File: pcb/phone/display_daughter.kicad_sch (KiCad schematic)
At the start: 5 parts

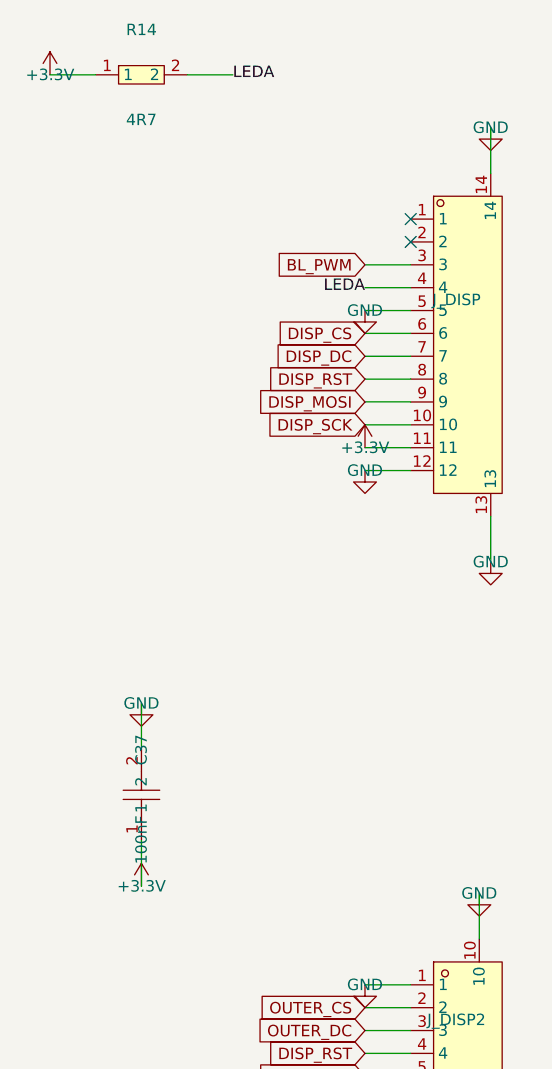
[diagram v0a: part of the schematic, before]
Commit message: User edits: keypad rewiring, sheet reorder, ERC severity reverts, R24 fix
Keypad (keypad.kicad_sch):
- Rotated all 20 switches 270 degrees for vertical contact orientation
- Wired all 4 pins on each switch (pins 1&2 to column, pins 3&4 to row)
- Removed all 37 no_connect markers on pins 3&4
- Cleaned up to 25.4mm (1-inch) grid spacing
- Added pull-down resistors to all 4 columns (was only KEY_COL3)

Root sheet (phone.kicad_sch):
- Reordered sub-sheet blocks (Display_Daughter before SIM_SD)
- Cleaned up PWR_FLAG symbol formatting/indentation
- Reordered PWR_FLAG and +BATT symbol placement

MCU sheet (mcu.kicad_sch):
- Repositioned +3.3V power symbol (#PWR32) at pin 190.5,200.66

Project settings (phone.kicad_pro):
- Reverted ERC suppressions: endpoint_off_grid, isolated_pin_label,
  lib_symbol_mismatch back to warning (want actual fixes, not ignores)
- Added SW2-20 to used designators
- Reordered sheets list (Display_Daughter before SIM_SD)

Other sheets (codec, display, display_daughter, sim_sd):
- KiCad editor reformatting upon save

Generated with [Devin](https://devin.ai)

Co-Authored-By: Devin <158243242+devin-ai-integration[bot]@users.noreply.github.com>
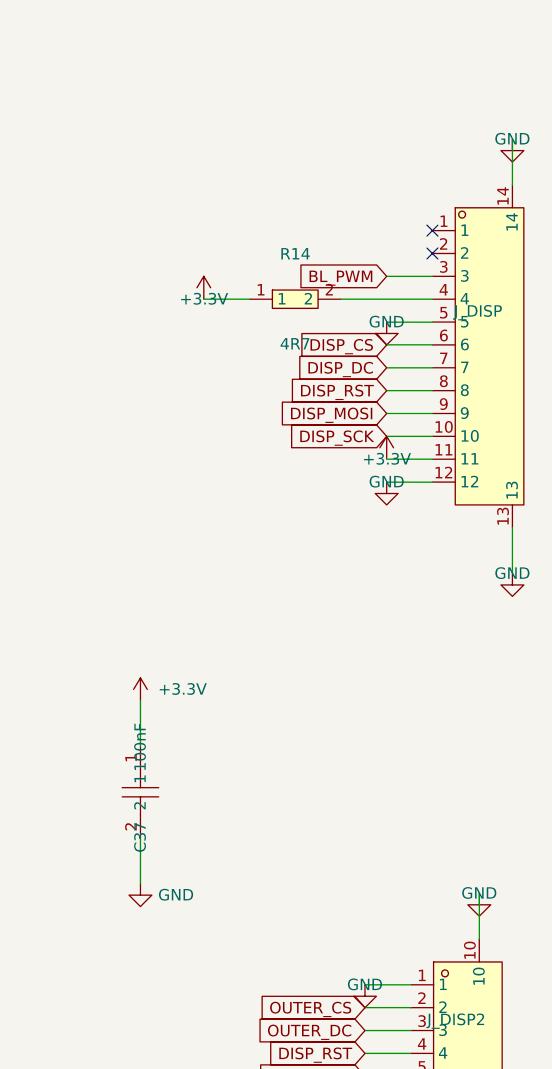
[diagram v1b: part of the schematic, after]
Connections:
- net LEDA: no longer names the net of J_DISP.4, R14.2
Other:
- moved on the sheet: C37, J_DISP, R14

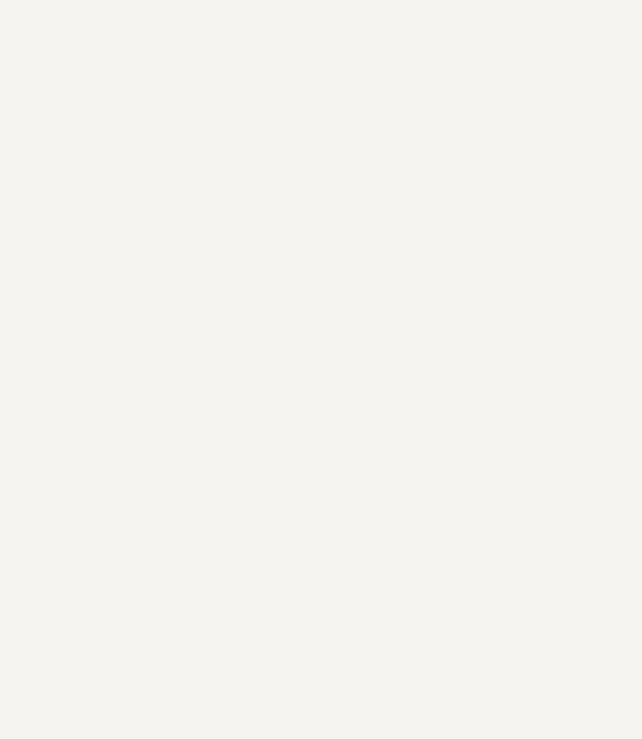
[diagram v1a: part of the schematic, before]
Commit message: Add J_HINGE2 hinge connector to display daughterboard
The display daughterboard (display_daughter.kicad_sch) was missing its
hinge connector — it had J_DISP, J_DISP2, and J_EARPIECE but no connector
to receive the flex cable from the main board's J_HINGE.

Added J_HINGE2 (connectors:0.5K-HX-14PWB, 14-pin 0.5mm FPC) at (130, 130)
with the same pin-to-net mapping as J_HINGE on the main board:

  Pin 1: +3.3V       Pin 8: OUTER_CS     Pin 15: GND (mounting)
  Pin 2: GND         Pin 9: OUTER_DC     Pin 16: GND (mounting)
  Pin 3: DISP_MOSI   Pin 10: BL_PWM
  Pin 4: DISP_SCK    Pin 11: NC (spare)
  Pin 5: DISP_CS     Pin 12: EARPIECE+
  Pin 6: DISP_DC     Pin 13: EARPIECE-
  Pin 7: DISP_RST    Pin 14: GND

All signal pins connect to existing global labels on the daughterboard
sheet (DISP_MOSI, DISP_SCK, DISP_CS, DISP_DC, DISP_RST, OUTER_CS,
OUTER_DC, BL_PWM, EARPIECE+, EARPIECE-). Power pins connect to +3.3V
and GND power symbols. Pin 11 (spare) has a no_connect marker.

Also added the 0.5K-HX-14PWB lib_symbol definition to the daughterboard
sheet (extracted from display.kicad_sch).

ERC: 0 errors, 196 warnings (152 endpoint_off_grid from FPC pin pitch,
35 lib_symbol_mismatch pre-existing, 9 isolated_pin_label pre-existing).

Generated with [Devin](https://devin.ai)

Co-Authored-By: Devin <158243242+devin-ai-integration[bot]@users.noreply.github.com>
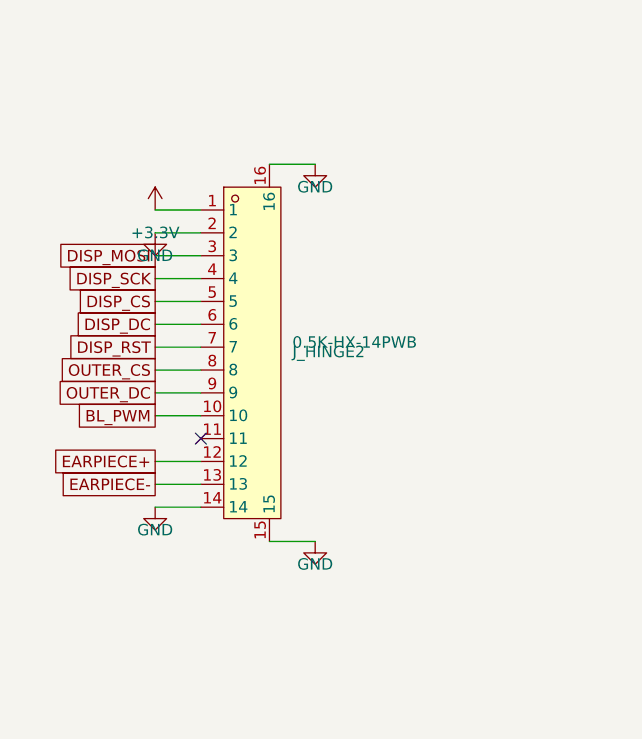
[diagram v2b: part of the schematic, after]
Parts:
- added J_HINGE2: 0.5K-HX-14PWB, symbol connectors:0.5K-HX-14PWB
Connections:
- net +3.3V: now also J_HINGE2.1
- net BL_PWM: now also J_HINGE2.10
- net DISP_CS: now also J_HINGE2.5
- net DISP_DC: now also J_HINGE2.6
- net DISP_MOSI: now also J_HINGE2.3
- net DISP_RST: now also J_HINGE2.7
- net DISP_SCK: now also J_HINGE2.4
- net EARPIECE+: now also J_HINGE2.12
- net EARPIECE-: now also J_HINGE2.13
- net GND: now also J_HINGE2.14, J_HINGE2.15, J_HINGE2.16, J_HINGE2.2
- net OUTER_CS: now also J_HINGE2.8
- net OUTER_DC: now also J_HINGE2.9
- no-connect marks 2 -> 3
